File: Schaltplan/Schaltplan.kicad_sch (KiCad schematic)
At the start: 15 parts, among them P1 USB_C_Plug_USB2.0, P2 USB_C_Plug_USB2.0, P3 USB_C_Plug_USB2.0, U1 ACS712xLCTR-05B, U2 LM2596S, U3 DS18B20, U4 DS18B20, U5 LM2596S, U6 DS3502, U7 DS3502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

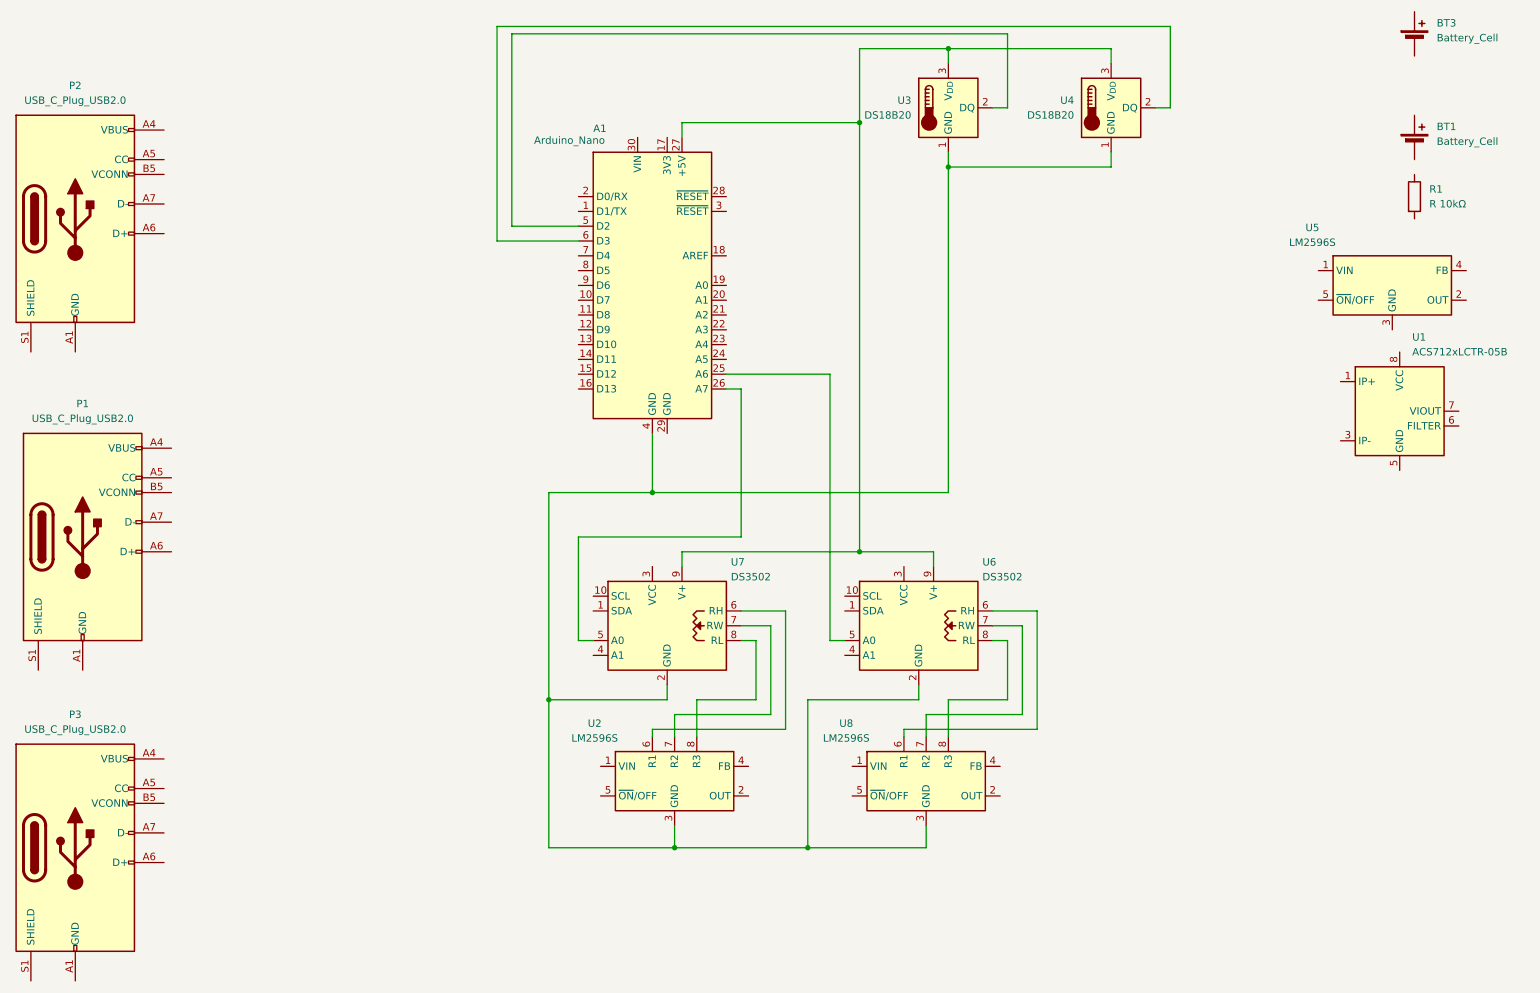
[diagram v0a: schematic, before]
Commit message: Update Schaltplan with new junctions and reposition components
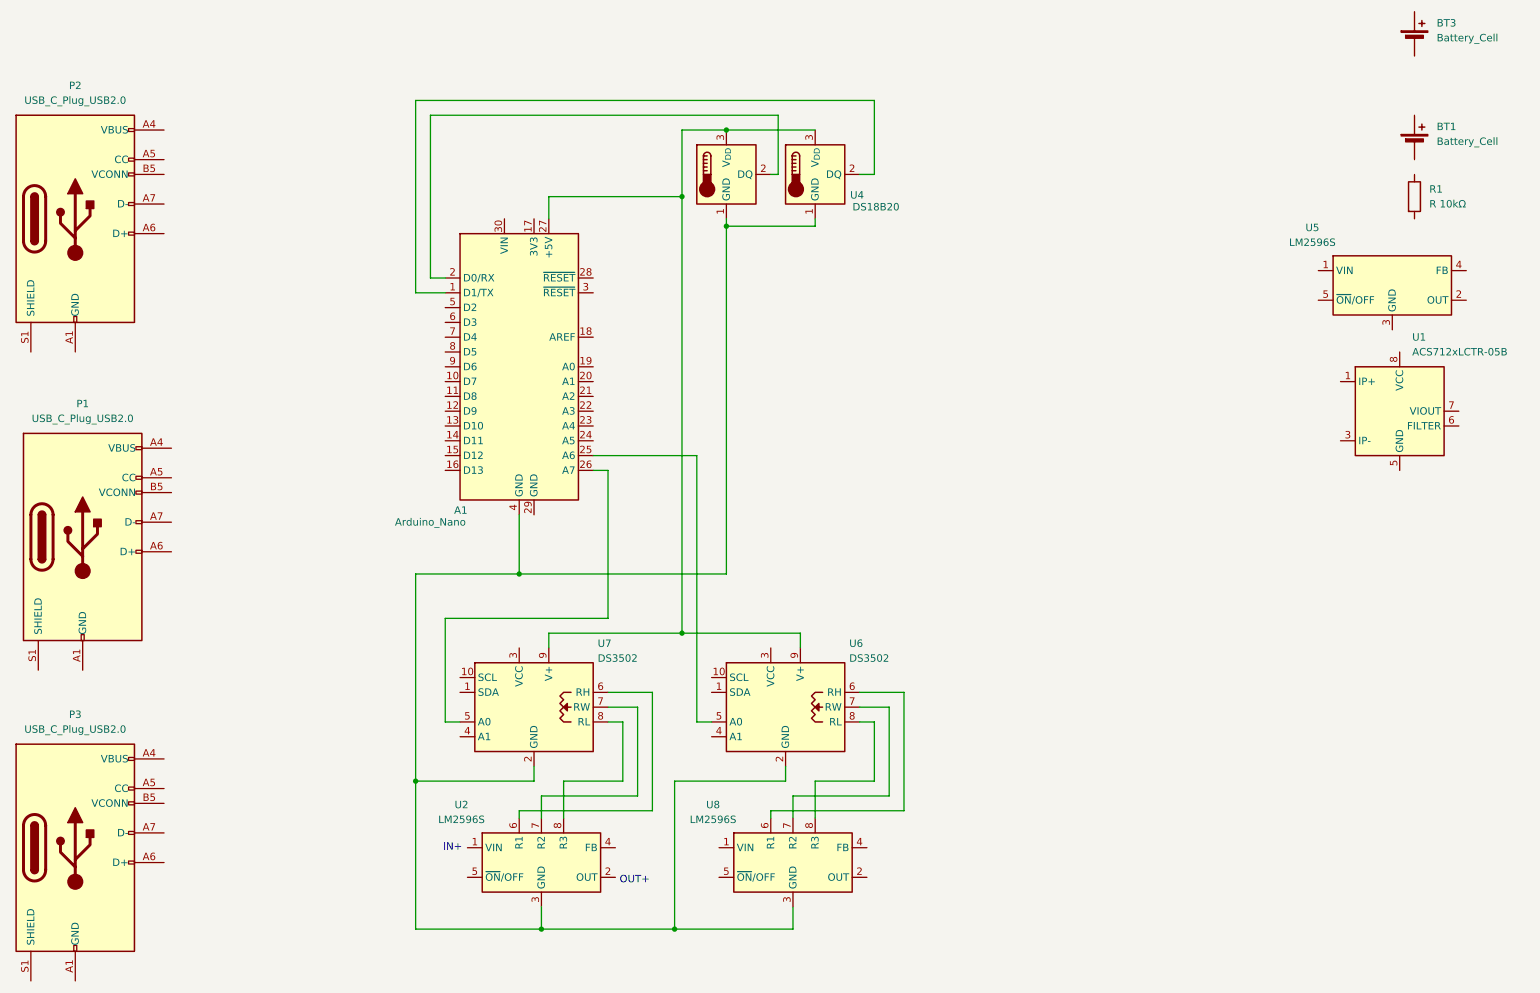
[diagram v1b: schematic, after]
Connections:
- net at U3.2 (DQ): now also A1.2 (D0/RX); no longer A1.5 (D2)
- net at U4.2 (DQ): now also A1.1 (D1/TX); no longer A1.6 (D3)
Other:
- note added: "IN+"
- note added: "OUT+"
- moved on the sheet: A1, U2, U4, U6, U7, U8
